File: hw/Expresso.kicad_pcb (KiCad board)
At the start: 4 copper layers, 85.3 x 75.7 mm, 108 parts, among them J1 USB_C_Receptacle_USB2.0_16P, J2 Midi In, J3 Midi Out, J5 Debug, J6 Exp, J7 Exp, J8 Exp, J9 Exp, SW1 Reset, SW2 Boot0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

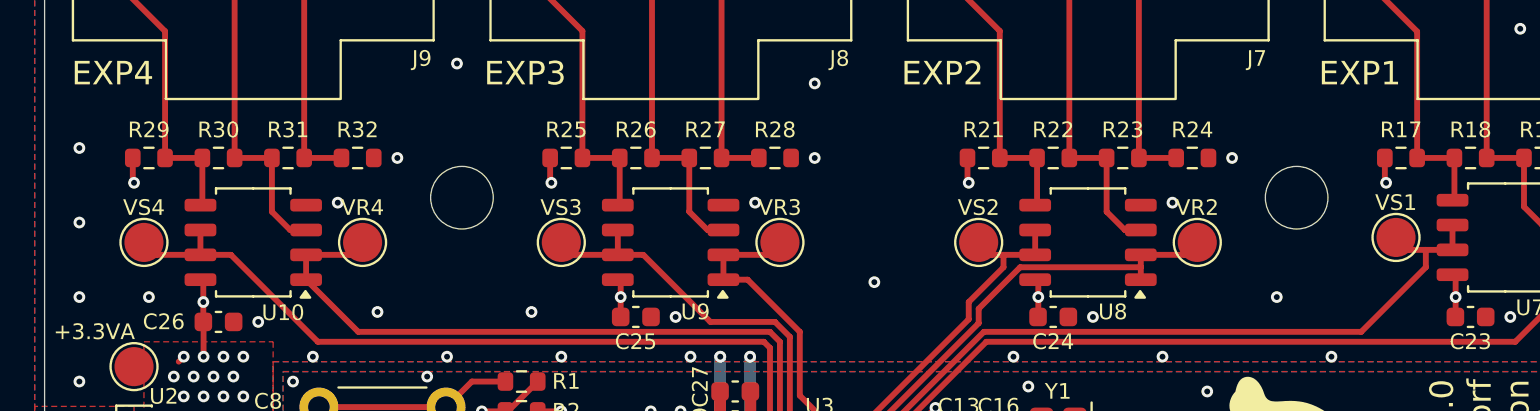
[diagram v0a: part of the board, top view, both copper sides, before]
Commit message: fixed input range issue
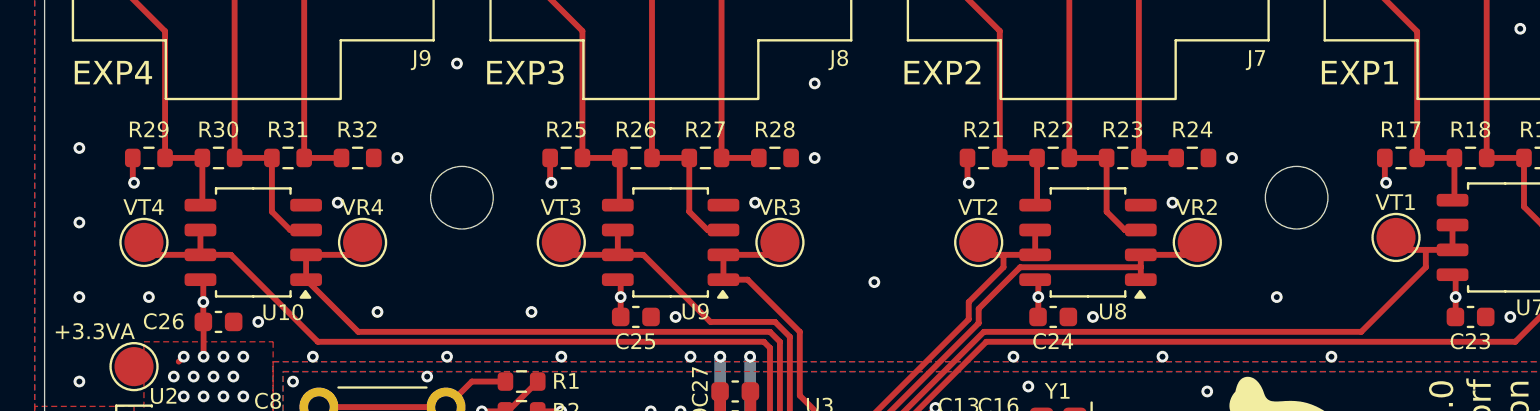
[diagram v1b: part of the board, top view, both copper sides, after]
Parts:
- TP11, TP13, TP15, TP17: value VS -> VT
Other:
- board text added: "VT1"
- board text added: "VT2"
- board text added: "VT3"
- board text added: "VT4"
- board text removed: "VS1"
- board text removed: "VS2"
- board text removed: "VS3"
- board text removed: "VS4"
